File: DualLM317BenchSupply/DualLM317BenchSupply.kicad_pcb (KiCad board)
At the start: 2 copper layers, 99.1 x 99.7 mm, 52 parts, among them CON101 BARREL_JACK, CON102 BARREL_JACK, P101 Vout+, P102 Vout-, SW101 SPDT, SW102 SPDT, SW103 SPDT, SW201 DP6T, U101 7812, U102 LM317, U103 LM317, U104 7805

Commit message: updating gerbers
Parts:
- moved D103 16.6 mm to (207.6, 209.6), turned to 270 degrees
- moved C109 7.62 mm to (233.7, 201.3)
- moved C104 7.43 mm to (225.4, 155.6), turned to 180 degrees
- moved RV101 7.24 mm to (222.9, 133.3)
- moved C102 6.99 mm to (210.2, 155.6), turned to 0 degrees
- moved R101 5.85 mm to (212.7, 212.7), turned to 0 degrees
- moved DS102 4.44 mm to (217.8, 186.7)
- moved C107 4.26 mm to (202.6, 177.2), turned to 270 degrees
- moved C108 3.86 mm to (226.1, 181.0)
- moved C110 3.81 mm to (217.8, 156.8)
- moved DS101 3.81 mm to (217.8, 171.4)
- moved RV102 3.81 mm to (217.8, 205.7)
- moved U101 3.81 mm to (208.9, 161.9)
- moved U104 3.81 mm to (221.6, 161.9)
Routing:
- net N-0000018: track 190.1 -> 217.0 mm
- net N-000007: track 56.2 -> 69.9 mm
- net 5V: track 83.9 -> 93.7 mm
- net N-0000014: track 31.4 -> 21.9 mm
- net N-000006: track 104.3 -> 107.4 mm
- net N-0000015: track 3.18 -> 5.34 mm
- net 12V: track 13.2 -> 12.7 mm

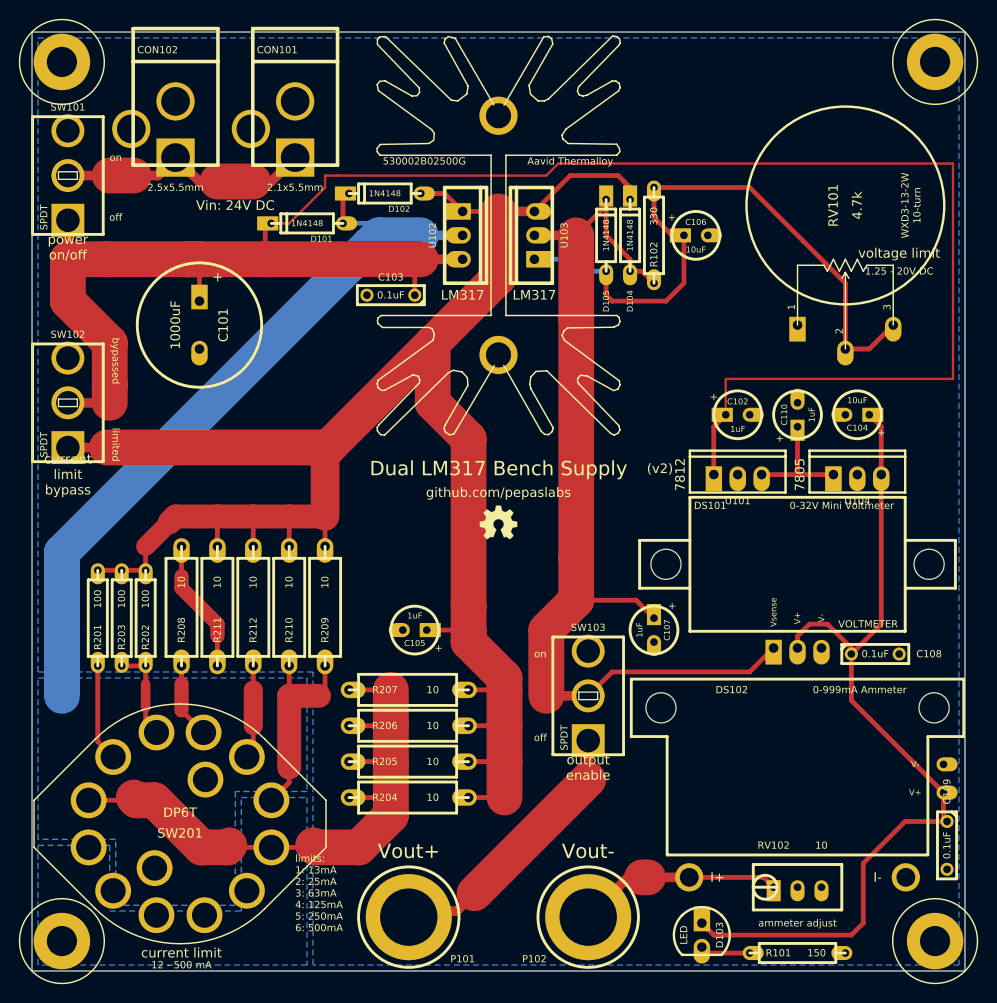
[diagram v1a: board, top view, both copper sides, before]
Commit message: using fills instead of traces for high current areas
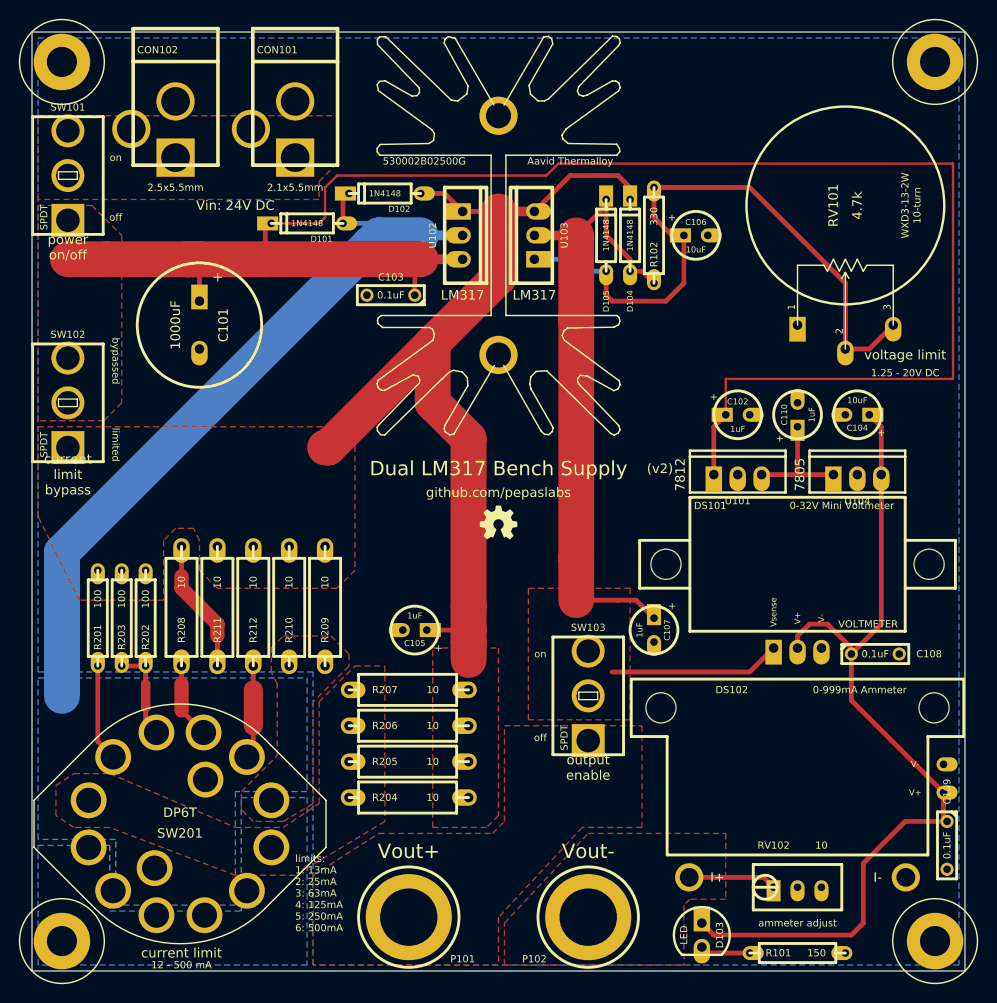
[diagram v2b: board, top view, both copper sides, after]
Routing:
- net /current_limit_r/R_LIM-: track 205.7 -> 99.0 mm
- net N-0000021: track 69.6 -> 0.00 mm
- net N-0000017: track 29.7 -> 0.00 mm
- net N-0000010: track 29.2 -> 0.00 mm
- net N-0000018: track 217.0 -> 192.5 mm
- net N-0000020: track 21.7 -> 0.00 mm
- net N-000006: track 107.4 -> 87.3 mm
- net N-0000014: track 21.9 -> 9.39 mm
- added copper zone on F.Cu, net /current_limit_r/R_LIM-
- added copper zone on F.Cu, net N-0000010
- added copper zone on F.Cu, net N-0000014
- added copper zone on F.Cu, net N-0000017
- added copper zone on F.Cu, net N-0000018
- added copper zone on F.Cu, net N-0000020
- added copper zone on F.Cu, net N-0000021
- added copper zone on F.Cu, net N-000006

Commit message: more tweaks to fills
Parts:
- moved C107 15.5 mm to (187.3, 174.6), turned to 180 degrees
- moved C105 9.09 mm to (187.3, 180.3)
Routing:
- net N-000006: track 87.3 -> 48.4 mm
- net /current_limit_r/R_LIM-: track 99.0 -> 78.9 mm
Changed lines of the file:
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@@
     (thickness 1.6)
     (drawings 27)
-    (tracks 133)
+    (tracks 127)
     (zones 0)
     (modules 52)
@@
   (page A3)
   (layers
-    (15 F.Cu signal)
+    (15 F.Cu signal hide)
     (0 B.Cu signal)
     (16 B.Adhes user)
@@
   )
   (setup
-    (last_trace_width 0.254)
+    (last_trace_width 0.508)
     (user_trace_width 0.508)
     (user_trace_width 1.016)
@@
   )
   (module ELCAP_10_20_V (layer F.Cu)
-    (at 178.435 178.435 180)
+    (at 187.325 180.34 180)
     (descr "Electrolytic Capacitor, vertical, 0.1\" pins, 0.2\" body")
     (tags CP)
@@
   )
   (module ELCAP_10_20_V (layer F.Cu)
-    (at 202.565 177.165 270)
+    (at 187.325 174.625 180)
     (descr "Electrolytic Capacitor, vertical, 0.1\" pins, 0.2\" body")
     (tags CP)
-    (fp_text reference C107 (at 1.27 -1.397 270) (layer F.SilkS)
-      (effects (font (size 0.635 0.635) (thickness 0.127)))
-    )
-    (fp_text value 1uF (at 1.27 1.524 270) (layer F.SilkS)
-      (effects (font (size 0.635 0.635) (thickness 0.127)))
-    )
-    (fp_text user + (at -1.27 -1.905 270) (layer F.SilkS)
+    (fp_text reference C107 (at 1.27 -1.397 180) (layer F.SilkS)
+      (effects (font (size 0.635 0.635) (thickness 0.127)))
+    )
+    (fp_text value 1uF (at 1.27 1.524 180) (layer F.SilkS)
+      (effects (font (size 0.635 0.635) (thickness 0.127)))
+    )
+    (fp_text user + (at -1.27 -1.905 180) (layer F.SilkS)
       (effects (font (size 0.762 0.762) (thickness 0.1524)))
     )
     (fp_circle (center 1.27 0) (end 3.81 0) (layer F.SilkS) (width 0.3048))
-    (pad 1 thru_hole rect (at 0 0 270) (size 2.2479 1.4986) (drill 0.8128 (offset -0.37465 0))
+    (pad 1 thru_hole rect (at 0 0 180) (size 2.2479 1.4986) (drill 0.8128 (offset -0.37465 0))
       (layers *.Cu *.Mask F.SilkS)
       (net 18 N-000006)
     )
-    (pad 2 thru_hole oval (at 2.54 0 270) (size 2.2479 1.4986) (drill 0.8128 (offset 0.37465 0))
+    (pad 2 thru_hole oval (at 2.54 0 180) (size 2.2479 1.4986) (drill 0.8128 (offset 0.37465 0))
       (layers *.Cu *.Mask F.SilkS)
       (net 5 GND)
@@
   (segment (start 172.4025 137.4775) (end 139.7 170.18) (width 3.81) (layer B.Cu) (net 1))
   (segment (start 177.8 136.525) (end 173.355 136.525) (width 3.81) (layer B.Cu) (net 1))
-  (segment (start 182.88 181.61) (end 182.88 179.705) (width 3.81) (layer F.Cu) (net 2))
-  (segment (start 182.88 179.705) (end 182.88 178.435) (width 3.81) (layer F.Cu) (net 2))
-  (segment (start 178.435 178.435) (end 182.88 178.435) (width 0.508) (layer F.Cu) (net 2))
-  (segment (start 182.88 175.895) (end 182.88 178.435) (width 3.81) (layer F.Cu) (net 2))
-  (segment (start 182.88 158.115) (end 182.88 175.895) (width 3.81) (layer F.Cu) (net 2))
+  (segment (start 187.325 180.34) (end 187.325 182.245) (width 0.508) (layer F.Cu) (net 2) (status 400000))
+  (segment (start 186.69 182.88) (end 185.42 182.88) (width 0.508) (layer F.Cu) (net 2))
+  (segment (start 187.325 182.245) (end 186.69 182.88) (width 0.508) (layer F.Cu) (net 2))
+  (segment (start 182.88 158.115) (end 182.88 161.925) (width 3.81) (layer F.Cu) (net 2))
   (segment (start 179.07 147.955) (end 179.07 154.305) (width 3.81) (layer F.Cu) (net 2))
   (segment (start 182.88 158.115) (end 179.07 154.305) (width 3.81) (layer F.Cu) (net 2))
@@
   (segment (start 148.59 184.15) (end 148.59 182.245) (width 0.508) (layer F.Cu) (net 17))
   (segment (start 146.05 182.245) (end 148.59 182.245) (width 0.508) (layer F.Cu) (net 17))
-  (segment (start 200.66 175.26) (end 202.565 177.165) (width 0.508) (layer F.Cu) (net 18))
-  (segment (start 198.755 175.26) (end 200.66 175.26) (width 0.508) (layer F.Cu) (net 18))
-  (segment (start 194.31 175.26) (end 198.755 175.26) (width 0.508) (layer F.Cu) (net 18))
   (segment (start 215.265 180.34) (end 212.725 182.88) (width 0.508) (layer F.Cu) (net 18))
   (segment (start 212.725 182.88) (end 198.12 182.88) (width 0.508) (layer F.Cu) (net 18))
@@
   (segment (start 197.485 133.35) (end 194.31 136.525) (width 0.508) (layer F.Cu) (net 18))
   (segment (start 189.865 136.525) (end 194.31 136.525) (width 1.016) (layer F.Cu) (net 18))
-  (segment (start 194.31 170.815) (end 194.31 175.26) (width 3.81) (layer F.Cu) (net 18))
-  (segment (start 194.31 145.415) (end 194.31 170.815) (width 3.81) (layer F.Cu) (net 18))
   (segment (start 194.31 136.525) (end 194.31 145.415) (width 3.81) (layer F.Cu) (net 18))
   (segment (start 218.44 137.16) (end 222.885 141.605) (width 0.508) (layer F.Cu) (net 19))
@@
     (polygon
       (pts
-        (xy 186.055 198.12) (xy 184.785 199.39) (xy 179.07 199.39) (xy 179.07 182.245) (xy 179.07 180.34)
-        (xy 186.055 180.34)
+        (xy 186.055 198.12) (xy 184.785 199.39) (xy 174.625 199.39) (xy 174.625 159.385) (xy 186.055 159.385)
       )
     )
@@
         (xy 170.815 172.085) (xy 168.91 173.99) (xy 156.21 173.99) (xy 154.305 172.085) (xy 154.305 168.91)
         (xy 153.67 167.64) (xy 151.765 167.64) (xy 150.495 168.91) (xy 150.495 175.26) (xy 141.605 175.26)
-        (xy 137.16 166.37) (xy 137.16 156.845) (xy 170.815 156.845)
+        (xy 137.16 166.37) (xy 137.16 157.48) (xy 170.815 157.48)
       )
     )
@@
     (polygon
       (pts
-        (xy 146.05 154.305) (xy 144.145 156.21) (xy 137.16 156.21) (xy 137.16 133.35) (xy 142.875 133.35)
+        (xy 146.05 154.305) (xy 143.51 156.845) (xy 137.16 156.845) (xy 137.16 133.35) (xy 142.875 133.35)
         (xy 146.05 136.525)
       )
@@
     (polygon
       (pts
-        (xy 200.025 187.96) (xy 189.23 187.96) (xy 189.23 173.99) (xy 200.025 173.99)
+        (xy 200.025 187.96) (xy 186.69 187.96) (xy 186.69 152.4) (xy 189.23 152.4) (xy 189.23 144.78)
+        (xy 200.025 144.78)
       )
     )

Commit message: updating barrell jack footprints
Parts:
- moved CON101 12.7 mm to (151.8, 128.3)
- moved CON102 12.7 mm to (164.5, 128.3)
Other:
- board text added: "13 - 500 mA"
- board text removed: "12 - 500 mA"
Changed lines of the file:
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@@
   )
   (setup
-    (last_trace_width 0.508)
+    (last_trace_width 0.254)
     (user_trace_width 0.508)
     (user_trace_width 1.016)
@@
     )
   )
-  (module BARREL_JACK_21x55 (layer F.Cu)
-    (at 164.465 128.27 270)
-    (descr "DC Barrel Jack, 2.1x5.5mm")
-    (tags "Power Jack")
-    (fp_text reference CON101 (at -11.43 1.905 360) (layer F.SilkS)
-      (effects (font (size 0.762 0.762) (thickness 0.1524)))
-    )
-    (fp_text value BARREL_JACK (at -4.445 -5.334 270) (layer F.SilkS) hide
-      (effects (font (size 1.016 1.016) (thickness 0.2032)))
-    )
-    (fp_text user 2.1x5.5mm (at 3.175 0 360) (layer F.SilkS)
-      (effects (font (size 0.762 0.762) (thickness 0.1524)))
-    )
-    (fp_line (start -10.1981 -4.50088) (end -10.1981 4.50088) (layer F.SilkS) (width 0.381))
-    (fp_line (start -13.69822 -4.50088) (end -13.69822 4.50088) (layer F.SilkS) (width 0.381))
-    (fp_line (start -13.69822 4.50088) (end 0.80264 4.50088) (layer F.SilkS) (width 0.381))
-    (fp_line (start 0.80264 4.50088) (end 0.80264 -4.50088) (layer F.SilkS) (width 0.381))
-    (fp_line (start 0.80264 -4.50088) (end -13.69822 -4.50088) (layer F.SilkS) (width 0.381))
-    (pad 1 thru_hole rect (at 0 0 270) (size 4.064 4.064) (drill 3.048)
-      (layers *.Cu *.Mask F.SilkS)
-      (net 9 N-0000017)
-    )
-    (pad 2 thru_hole circle (at -5.969 0 270) (size 4.064 4.064) (drill 3.048)
-      (layers *.Cu *.Mask F.SilkS)
-      (net 5 GND)
-    )
-    (pad 3 thru_hole circle (at -3.048 4.699 270) (size 4.064 4.064) (drill 3.048)
-      (layers *.Cu *.Mask F.SilkS)
-      (net 5 GND)
-    )
-  )
   (module R_AXIAL_0W5 (layer F.Cu)
     (at 152.4 182.245 90)
@@
       (scale (xyz 0.4 0.4 0.4))
       (rotate (xyz 0 0 0))
-    )
-  )
-  (module BARREL_JACK_25x55 (layer F.Cu)
-    (at 151.765 128.27 270)
-    (descr "DC Barrel Jack, 2.5x5.5mm")
-    (tags "Power Jack")
-    (fp_text reference CON102 (at -11.43 1.905 360) (layer F.SilkS)
-      (effects (font (size 0.762 0.762) (thickness 0.1524)))
-    )
-    (fp_text value BARREL_JACK (at -4.445 -5.334 270) (layer F.SilkS) hide
-      (effects (font (size 1.016 1.016) (thickness 0.2032)))
-    )
-    (fp_text user 2.5x5.5mm (at 3.175 0 360) (layer F.SilkS)
-      (effects (font (size 0.762 0.762) (thickness 0.1524)))
-    )
-    (fp_line (start -10.1981 -4.50088) (end -10.1981 4.50088) (layer F.SilkS) (width 0.381))
-    (fp_line (start -13.69822 -4.50088) (end -13.69822 4.50088) (layer F.SilkS) (width 0.381))
-    (fp_line (start -13.69822 4.50088) (end 0.80264 4.50088) (layer F.SilkS) (width 0.381))
-    (fp_line (start 0.80264 4.50088) (end 0.80264 -4.50088) (layer F.SilkS) (width 0.381))
-    (fp_line (start 0.80264 -4.50088) (end -13.69822 -4.50088) (layer F.SilkS) (width 0.381))
-    (pad 1 thru_hole rect (at 0 0 270) (size 4.064 4.064) (drill 3.048)
-      (layers *.Cu *.Mask F.SilkS)
-      (net 9 N-0000017)
-    )
-    (pad 2 thru_hole circle (at -5.969 0 270) (size 4.064 4.064) (drill 3.048)
-      (layers *.Cu *.Mask F.SilkS)
-      (net 5 GND)
-    )
-    (pad 3 thru_hole circle (at -3.048 4.699 270) (size 4.064 4.064) (drill 3.048)
-      (layers *.Cu *.Mask F.SilkS)
-      (net 5 GND)
     )
   )
@@
     )
   )
+  (module BARREL_JACK_25x55 (layer F.Cu)
+    (at 164.465 128.27 270)
+    (descr "DC Barrel Jack, 2.5x5.5mm")
+    (tags "Power Jack")
+    (fp_text reference CON102 (at -7.62 5.461 270) (layer F.SilkS)
+      (effects (font (size 0.762 0.762) (thickness 0.1524)))
+    )
+    (fp_text value BARREL_JACK (at -4.445 -5.334 270) (layer F.SilkS) hide
+      (effects (font (size 1.016 1.016) (thickness 0.2032)))
+    )
+    (fp_text user 2.5x5.5mm (at 3.175 0 360) (layer F.SilkS)
+      (effects (font (size 0.762 0.762) (thickness 0.1524)))
+    )
+    (fp_line (start -10.1981 -4.50088) (end -10.1981 4.50088) (layer F.SilkS) (width 0.254))
+    (fp_line (start -13.69822 -4.50088) (end -13.69822 4.50088) (layer F.SilkS) (width 0.254))
+    (fp_line (start -13.69822 4.50088) (end 0.80264 4.50088) (layer F.SilkS) (width 0.254))
+    (fp_line (start 0.80264 4.50088) (end 0.80264 -4.50088) (layer F.SilkS) (width 0.254))
+    (fp_line (start 0.80264 -4.50088) (end -13.69822 -4.50088) (layer F.SilkS) (width 0.254))
+    (pad 1 thru_hole rect (at 0 0 270) (size 4.064 4.064) (drill 2.7432)
+      (layers *.Cu *.Mask F.SilkS)
+      (net 9 N-0000017)
+    )
+    (pad 2 thru_hole circle (at -5.969 0 270) (size 4.064 4.064) (drill 2.7432)
+      (layers *.Cu *.Mask F.SilkS)
+      (net 5 GND)
+    )
+    (pad 3 thru_hole circle (at -3.048 4.699 270) (size 4.064 4.064) (drill 2.7432)
+      (layers *.Cu *.Mask F.SilkS)
+      (net 5 GND)
+    )
+  )
+  (module BARREL_JACK_21x55 (layer F.Cu)
+    (at 151.765 128.27 270)
+    (descr "DC Barrel Jack, 2.1x5.5mm")
+    (tags "Power Jack")
+    (fp_text reference CON101 (at -7.62 5.461 270) (layer F.SilkS)
+      (effects (font (size 0.762 0.762) (thickness 0.1524)))
+    )
+    (fp_text value BARREL_JACK (at -4.445 -5.334 270) (layer F.SilkS) hide
+      (effects (font (size 1.016 1.016) (thickness 0.2032)))
+    )
+    (fp_text user 2.1x5.5mm (at 3.175 0 360) (layer F.SilkS)
+      (effects (font (size 0.762 0.762) (thickness 0.1524)))
+    )
+    (fp_line (start -10.1981 -4.50088) (end -10.1981 4.50088) (layer F.SilkS) (width 0.254))
+    (fp_line (start -13.69822 -4.50088) (end -13.69822 4.50088) (layer F.SilkS) (width 0.254))
+    (fp_line (start -13.69822 4.50088) (end 0.80264 4.50088) (layer F.SilkS) (width 0.254))
+    (fp_line (start 0.80264 4.50088) (end 0.80264 -4.50088) (layer F.SilkS) (width 0.254))
+    (fp_line (start 0.80264 -4.50088) (end -13.69822 -4.50088) (layer F.SilkS) (width 0.254))
+    (pad 1 thru_hole rect (at 0 0 270) (size 4.064 4.064) (drill 2.7432)
+      (layers *.Cu *.Mask F.SilkS)
+      (net 9 N-0000017)
+    )
+    (pad 2 thru_hole circle (at -5.969 0 270) (size 4.064 4.064) (drill 2.7432)
+      (layers *.Cu *.Mask F.SilkS)
+      (net 5 GND)
+    )
+    (pad 3 thru_hole circle (at -3.048 4.699 270) (size 4.064 4.064) (drill 2.7432)
+      (layers *.Cu *.Mask F.SilkS)
+      (net 5 GND)
+    )
+  )
   (gr_text "(v2)" (at 168.91 161.29) (layer B.SilkS)
     (effects (font (size 1.016 1.016) (thickness 0.2032)) (justify mirror))
@@
     (effects (font (size 1.016 1.016) (thickness 0.2032)))
   )
-  (gr_text "12 - 500 mA" (at 152.4 213.995) (layer F.SilkS)
+  (gr_text "13 - 500 mA" (at 152.4 213.995) (layer F.SilkS)
     (effects (font (size 0.762 0.762) (thickness 0.1524)))
   )
@@
   (segment (start 172.4025 137.4775) (end 139.7 170.18) (width 3.81) (layer B.Cu) (net 1))
   (segment (start 177.8 136.525) (end 173.355 136.525) (width 3.81) (layer B.Cu) (net 1))
-  (segment (start 187.325 180.34) (end 187.325 182.245) (width 0.508) (layer F.Cu) (net 2) (status 400000))
+  (segment (start 187.325 180.34) (end 187.325 182.245) (width 0.508) (layer F.Cu) (net 2))
   (segment (start 186.69 182.88) (end 185.42 182.88) (width 0.508) (layer F.Cu) (net 2))
   (segment (start 187.325 182.245) (end 186.69 182.88) (width 0.508) (layer F.Cu) (net 2))
